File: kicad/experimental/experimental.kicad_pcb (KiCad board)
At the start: 2 copper layers, 39.7 x 27.4 mm, 44 parts, among them J1 PWR_IN, J2 SIG_IN, J3 SIG_OUT, J4 PWR_IN, J5 SIG_IN, J6 SPI, U1 OPA2197, U2 OPA2197, U3 L78L05, U4 AD7682BCP

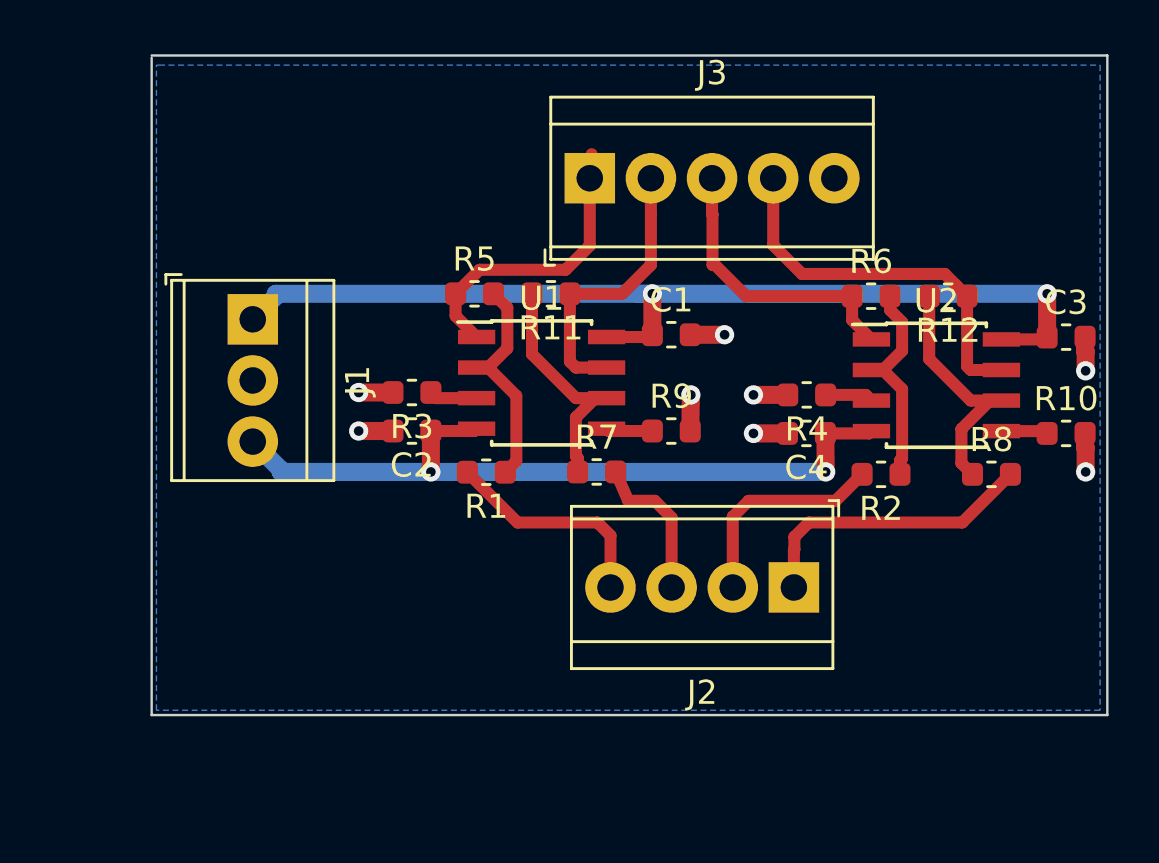
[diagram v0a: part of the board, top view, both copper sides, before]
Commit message: designed pcb for experimental buffer board
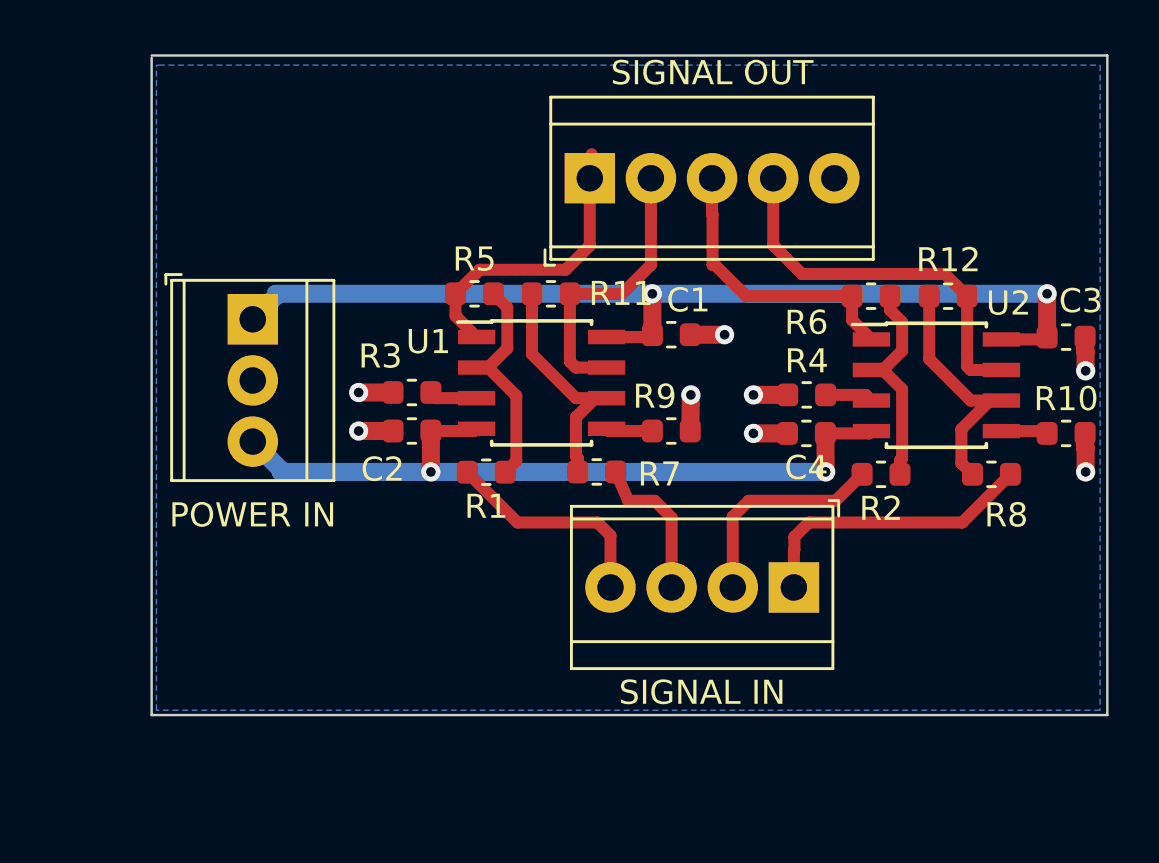
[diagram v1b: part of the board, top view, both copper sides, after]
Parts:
- POWER IN: renamed from J1
- SIGNAL IN: renamed from J2
- SIGNAL OUT: renamed from J3
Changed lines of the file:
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@@
     (35 F.Paste user)
     (36 B.SilkS user)
-    (37 F.SilkS user hide)
+    (37 F.SilkS user)
     (38 B.Mask user)
     (39 F.Mask user)
@@
     (tags "SOIC 1.27")
     (attr smd)
-    (fp_text reference U2 (at 0 -3.5) (layer F.SilkS)
+    (fp_text reference U2 (at 3 -3.4) (layer F.SilkS)
       (effects (font (size 1 1) (thickness 0.15)))
     )
@@
     (tags "SOIC 1.27")
     (attr smd)
-    (fp_text reference U1 (at 0 -3.5) (layer F.SilkS)
+    (fp_text reference U1 (at -4.7 -1.7) (layer F.SilkS)
       (effects (font (size 1 1) (thickness 0.15)))
     )
@@
     (tags resistor)
     (attr smd)
-    (fp_text reference R12 (at 0 -1.43) (layer F.SilkS)
+    (fp_text reference R12 (at -0.0125 1.5) (layer F.SilkS)
       (effects (font (size 1 1) (thickness 0.15)))
     )
@@
     (tags resistor)
     (attr smd)
-    (fp_text reference R11 (at 0 -1.43) (layer F.SilkS)
+    (fp_text reference R11 (at -2.9125 0) (layer F.SilkS)
       (effects (font (size 1 1) (thickness 0.15)))
     )
@@
     (tags resistor)
     (attr smd)
-    (fp_text reference R9 (at 0 -1.43) (layer F.SilkS)
+    (fp_text reference R9 (at -0.6875 -1.43) (layer F.SilkS)
       (effects (font (size 1 1) (thickness 0.15)))
     )
@@
     (tags resistor)
     (attr smd)
-    (fp_text reference R8 (at 0 -1.43) (layer F.SilkS)
+    (fp_text reference R8 (at 0.6125 1.7) (layer F.SilkS)
       (effects (font (size 1 1) (thickness 0.15)))
     )
@@
     (tags resistor)
     (attr smd)
-    (fp_text reference R7 (at 0 -1.43) (layer F.SilkS)
+    (fp_text reference R7 (at 2.6125 0.1) (layer F.SilkS)
       (effects (font (size 1 1) (thickness 0.15)))
     )
@@
     (tags resistor)
     (attr smd)
-    (fp_text reference R6 (at 0 -1.43) (layer F.SilkS)
+    (fp_text reference R6 (at -2.6875 1.1) (layer F.SilkS)
       (effects (font (size 1 1) (thickness 0.15)))
     )
@@
     (tags resistor)
     (attr smd)
-    (fp_text reference R4 (at 0 -1.43) (layer F.SilkS)
+    (fp_text reference R4 (at 0 1.4) (layer F.SilkS)
       (effects (font (size 1 1) (thickness 0.15)))
     )
@@
     (tags resistor)
     (attr smd)
-    (fp_text reference R3 (at 0 -1.43) (layer F.SilkS)
+    (fp_text reference R3 (at 1.3125 1.5) (layer F.SilkS)
       (effects (font (size 1 1) (thickness 0.15)))
     )
@@
     (descr "Terminal Block TE 282834-5, 5 pins, pitch 2.54mm, size 13.16x6.5mm^2, drill diamater 1.1mm, pad diameter 2.1mm, see http://www.te.com/commerce/DocumentDelivery/DDEController?Action=showdoc&DocId=Customer+Drawing%7F282834%7FC1%7Fpdf%7FEnglish%7FENG_CD_282834_C1.pdf, script-generated using https://github.com/pointhi/kicad-footprint-generator/scripts/TerminalBlock_TE-Connectivity")
     (tags "THT Terminal Block TE 282834-5 pitch 2.54mm size 13.16x6.5mm^2 drill 1.1mm pad 2.1mm")
-    (fp_text reference J3 (at 5.08 -4.37) (layer F.SilkS)
+    (fp_text reference "SIGNAL OUT" (at 5.08 -4.37) (layer F.SilkS)
       (effects (font (size 1 1) (thickness 0.15)))
     )
@@
     (descr "Terminal Block TE 282834-4, 4 pins, pitch 2.54mm, size 10.620000000000001x6.5mm^2, drill diamater 1.1mm, pad diameter 2.1mm, see http://www.te.com/commerce/DocumentDelivery/DDEController?Action=showdoc&DocId=Customer+Drawing%7F282834%7FC1%7Fpdf%7FEnglish%7FENG_CD_282834_C1.pdf, script-generated using https://github.com/pointhi/kicad-footprint-generator/scripts/TerminalBlock_TE-Connectivity")
     (tags "THT Terminal Block TE 282834-4 pitch 2.54mm size 10.620000000000001x6.5mm^2 drill 1.1mm pad 2.1mm")
-    (fp_text reference J2 (at 3.81 -4.37) (layer F.SilkS)
+    (fp_text reference "SIGNAL IN" (at 3.81 -4.37) (layer F.SilkS)
       (effects (font (size 1 1) (thickness 0.15)))
     )
@@
     (descr "Terminal Block TE 282834-3, 3 pins, pitch 2.54mm, size 8.08x6.5mm^2, drill diamater 1.1mm, pad diameter 2.1mm, see http://www.te.com/commerce/DocumentDelivery/DDEController?Action=showdoc&DocId=Customer+Drawing%7F282834%7FC1%7Fpdf%7FEnglish%7FENG_CD_282834_C1.pdf, script-generated using https://github.com/pointhi/kicad-footprint-generator/scripts/TerminalBlock_TE-Connectivity")
     (tags "THT Terminal Block TE 282834-3 pitch 2.54mm size 8.08x6.5mm^2 drill 1.1mm pad 2.1mm")
-    (fp_text reference J1 (at 2.54 -4.37 90) (layer F.SilkS)
+    (fp_text reference "POWER IN" (at 8.14 0 180) (layer F.SilkS)
       (effects (font (size 1 1) (thickness 0.15)))
     )
@@
     (tags capacitor)
     (attr smd)
-    (fp_text reference C3 (at 0 -1.43) (layer F.SilkS)
+    (fp_text reference C3 (at 0.6125 -1.5) (layer F.SilkS)
       (effects (font (size 1 1) (thickness 0.15)))
     )
@@
     (tags capacitor)
     (attr smd)
-    (fp_text reference C2 (at 0 -1.43) (layer F.SilkS)
+    (fp_text reference C2 (at 1.2125 -1.6) (layer F.SilkS)
       (effects (font (size 1 1) (thickness 0.15)))
     )
@@
     (tags capacitor)
     (attr smd)
-    (fp_text reference C1 (at 0 -1.43) (layer F.SilkS)
+    (fp_text reference C1 (at 0.7125 -1.43) (layer F.SilkS)
       (effects (font (size 1 1) (thickness 0.15)))
     )
@@
     (connect_pads (clearance 0.508))
     (min_thickness 0.254)
-    (fill yes (arc_segments 32) (thermal_gap 0.508) (thermal_bridge_width 0.508))
+    (fill (arc_segments 32) (thermal_gap 0.508) (thermal_bridge_width 0.508))
     (polygon
       (pts

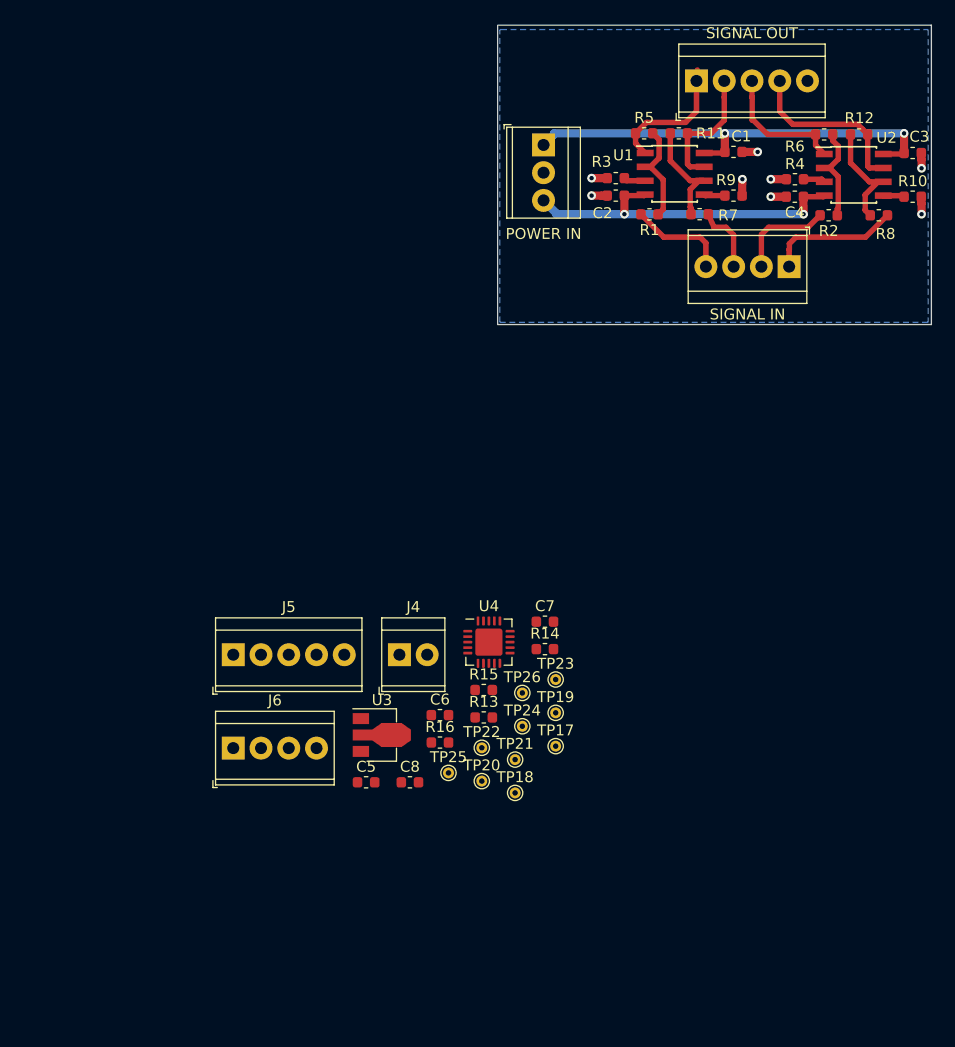
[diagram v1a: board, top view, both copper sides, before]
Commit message: completed pcb design of experimental buffer and adc
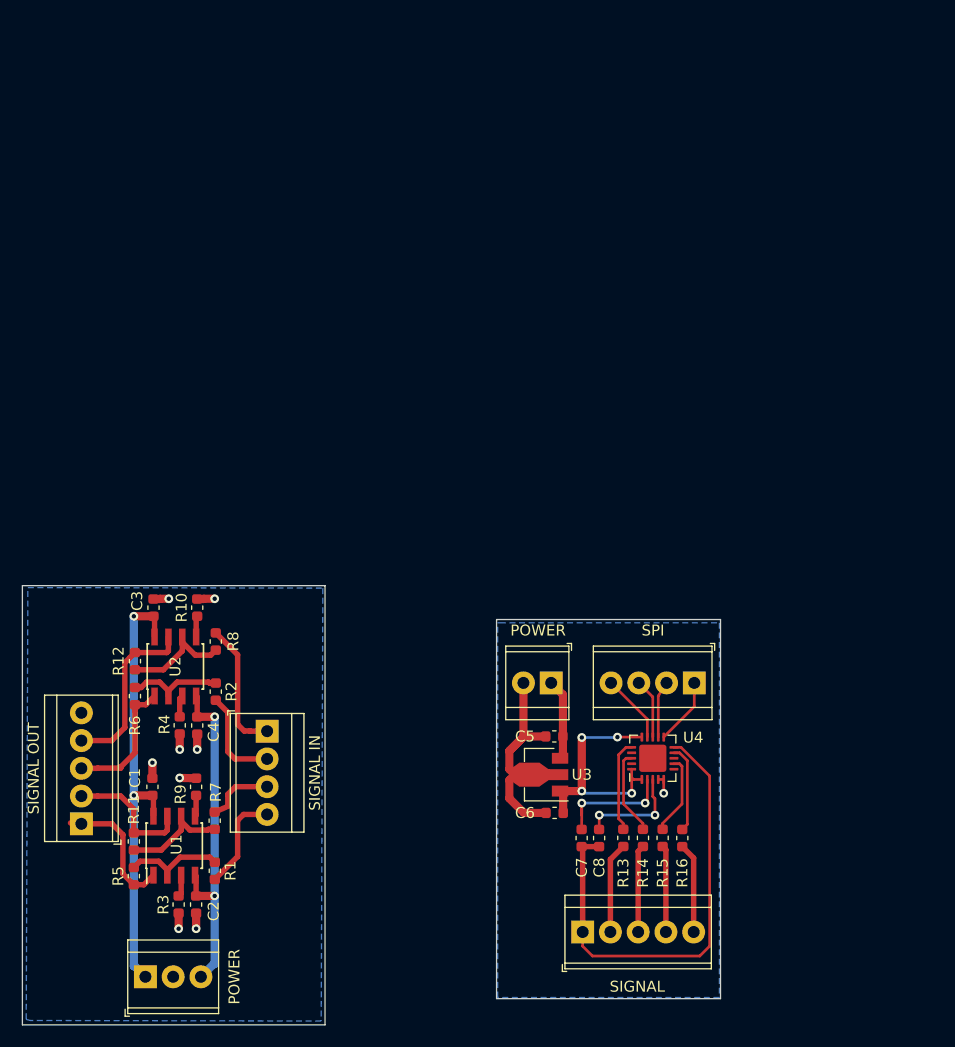
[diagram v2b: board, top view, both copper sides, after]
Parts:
- removed J4: PWR_IN, TerminalBlock_TE-Connectivity:TerminalBlock_TE_282834-2_1x02_P2.54mm_Horizontal
- removed J6: SPI, TerminalBlock_TE-Connectivity:TerminalBlock_TE_282834-4_1x04_P2.54mm_Horizontal
- removed TP17: +15V, TestPoint:TestPoint_THTPad_D1.0mm_Drill0.5mm
- removed TP18: +5V, TestPoint:TestPoint_THTPad_D1.0mm_Drill0.5mm
- removed TP19: IN0, TestPoint:TestPoint_THTPad_D1.0mm_Drill0.5mm
- removed TP20: IN1, TestPoint:TestPoint_THTPad_D1.0mm_Drill0.5mm
- removed TP21: IN2, TestPoint:TestPoint_THTPad_D1.0mm_Drill0.5mm
- removed TP22: IN3, TestPoint:TestPoint_THTPad_D1.0mm_Drill0.5mm
- removed TP23: REF, TestPoint:TestPoint_THTPad_D1.0mm_Drill0.5mm
- removed TP24: REFIN, TestPoint:TestPoint_THTPad_D1.0mm_Drill0.5mm
- removed TP25: COM, TestPoint:TestPoint_THTPad_D1.0mm_Drill0.5mm
- removed TP26: V+, TestPoint:TestPoint_THTPad_D1.0mm_Drill0.5mm
- added POWER: PWR_IN, TerminalBlock_TE-Connectivity:TerminalBlock_TE_282834-2_1x02_P2.54mm_Horizontal, F.Cu at (98.9, 84.6)
- added SPI: SPI, TerminalBlock_TE-Connectivity:TerminalBlock_TE_282834-4_1x04_P2.54mm_Horizontal, F.Cu at (112.0, 84.6)
- POWER: renamed from POWER IN
- moved SIGNAL OUT 88.3 mm to (55.9, 97.5), turned to 90 degrees
- moved POWER 84.4 mm to (61.8, 111.5), turned to 0 degrees
- moved R5 82.5 mm to (60.7, 102.3), turned to 90 degrees
- moved R12 82.0 mm to (60.8, 82.6), turned to 270 degrees
- moved R11 81.8 mm to (60.7, 99.1), turned to 270 degrees
- moved R6 81.4 mm to (60.8, 85.8), turned to 90 degrees
- moved C3 81.0 mm to (62.5, 77.7), turned to 90 degrees
- moved C1 78.8 mm to (62.4, 94.1), turned to 90 degrees
- moved R3 77.6 mm to (64.8, 104.9), turned to 270 degrees
- moved U2 76.7 mm to (64.5, 83.1), turned to 90 degrees
- moved U1 76.7 mm to (64.4, 99.5), turned to 90 degrees
- moved R10 75.5 mm to (66.5, 77.7), turned to 90 degrees
- moved C2 75.4 mm to (66.4, 104.9), turned to 270 degrees
- moved R4 75.3 mm to (64.9, 88.5), turned to 270 degrees
- moved R9 73.1 mm to (66.4, 94.1), turned to 90 degrees
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- renumbered J5 to SIGNAL
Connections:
- SIGNAL pad 1: /ADC/X1 -> GNDA
- SIGNAL pad 2: /ADC/X2 -> /ADC/X1
- SIGNAL pad 3: /ADC/Y1 -> /ADC/X2
- SIGNAL pad 4: /ADC/Y2 -> /ADC/Y1
- SIGNAL pad 5: GNDA -> /ADC/Y2
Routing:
- net GNDA: track 0.00 -> 43.0 mm
- net +5V: track 0.00 -> 22.4 mm, vias 0 -> 4
- net GND: track 11.7 -> 32.7 mm, vias 8 -> 9
- net Net-(C7-Pad1): track 0.00 -> 11.6 mm, vias 0 -> 2
- net Net-(C8-Pad1): track 0.00 -> 9.78 mm, vias 0 -> 2
- net /ADC/IN0: track 0.00 -> 8.47 mm
- net /ADC/X1: track 0.00 -> 8.31 mm
- net /ADC/Y2: track 0.00 -> 8.24 mm
- net /ADC/IN3: track 0.00 -> 8.01 mm
- net /ADC/X2: track 0.00 -> 8.01 mm
- net /ADC/Y1: track 0.00 -> 7.95 mm
- net /ADC/IN1: track 0.00 -> 7.84 mm
- net +15V: track 41.5 -> 48.9 mm
- net /ADC/IN2: track 0.00 -> 7.34 mm
- net /ADC/SDO: track 0.00 -> 6.34 mm
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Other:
- board size 39.7 x 27.4 mm -> 63.9 x 40.2 mm
